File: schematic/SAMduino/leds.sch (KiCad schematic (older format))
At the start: 32 parts, among them J10 Conn_02x11_Odd_Even, J11 Conn_02x09_Odd_Even, J12 Conn_02x09_Odd_Even, J13 Conn_01x02, J14 Conn_02x02_Odd_Even, J15 Conn_02x03_Odd_Even, J16 Conn_01x02, J17 Conn_02x03_Odd_Even, J18 Conn_02x02_Odd_Even, J19 Conn_02x03_Odd_Even, J20 Conn_01x08, J7 Conn_01x02, J8 Conn_01x02, J9 Conn_02x07_Odd_Even, SW1 SW_MEC_5E, SW2 SW_MEC_5E, SW3 MCLR, SW4 ERASE

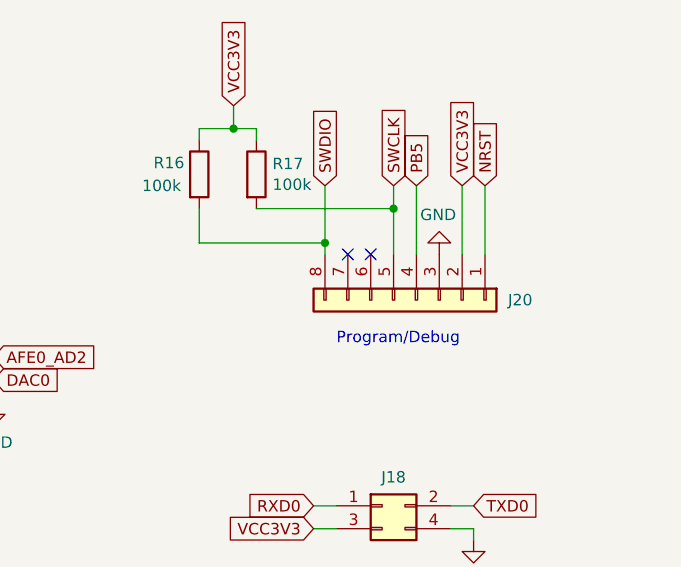
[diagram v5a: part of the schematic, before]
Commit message: Swapped program header to match PicKit4
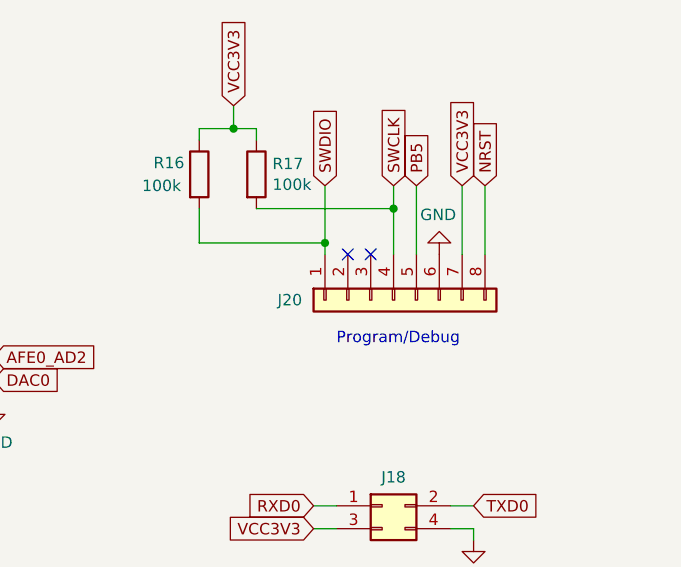
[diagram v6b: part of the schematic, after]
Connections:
- net GND: now also J20.6 (Pin_6); no longer J20.3 (Pin_3)
- net NRST: now also J20.8 (Pin_8); no longer J20.1 (Pin_1)
- net PB5: now also J20.5 (Pin_5); no longer J20.4 (Pin_4)
- net SWCLK: now also J20.4 (Pin_4); no longer J20.5 (Pin_5)
- net SWDIO: now also J20.1 (Pin_1); no longer J20.8 (Pin_8)
- net VCC3V3: now also J20.7 (Pin_7); no longer J20.2 (Pin_2)
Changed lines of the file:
@@
 L Connector_Generic:Conn_01x08 J20
 U 1 1 6166979A
-P 9350 3750
-F 0 "J20" V 9350 4150 50  0000 L CNN
-F 1 "Conn_01x08" H 9430 3651 50  0001 L CNN
-F 2 "Connector_PinHeader_2.54mm:PinHeader_1x08_P2.54mm_Horizontal" H 9350 3750 50  0001 C CNN
-F 3 "~" H 9350 3750 50  0001 C CNN
-	1    9350 3750
-	0    1    1    0
+P 9250 3750
+F 0 "J20" V 9250 4150 50  0000 L CNN
+F 1 "Conn_01x08" H 9330 3651 50  0001 L CNN
+F 2 "Connector_PinHeader_2.54mm:PinHeader_1x08_P2.54mm_Horizontal" H 9250 3750 50  0001 C CNN
+F 3 "~" H 9250 3750 50  0001 C CNN
+	1    9250 3750
+	0    -1   1    0
 $EndComp
 Text Notes 9000 3950 0    50   ~ 0

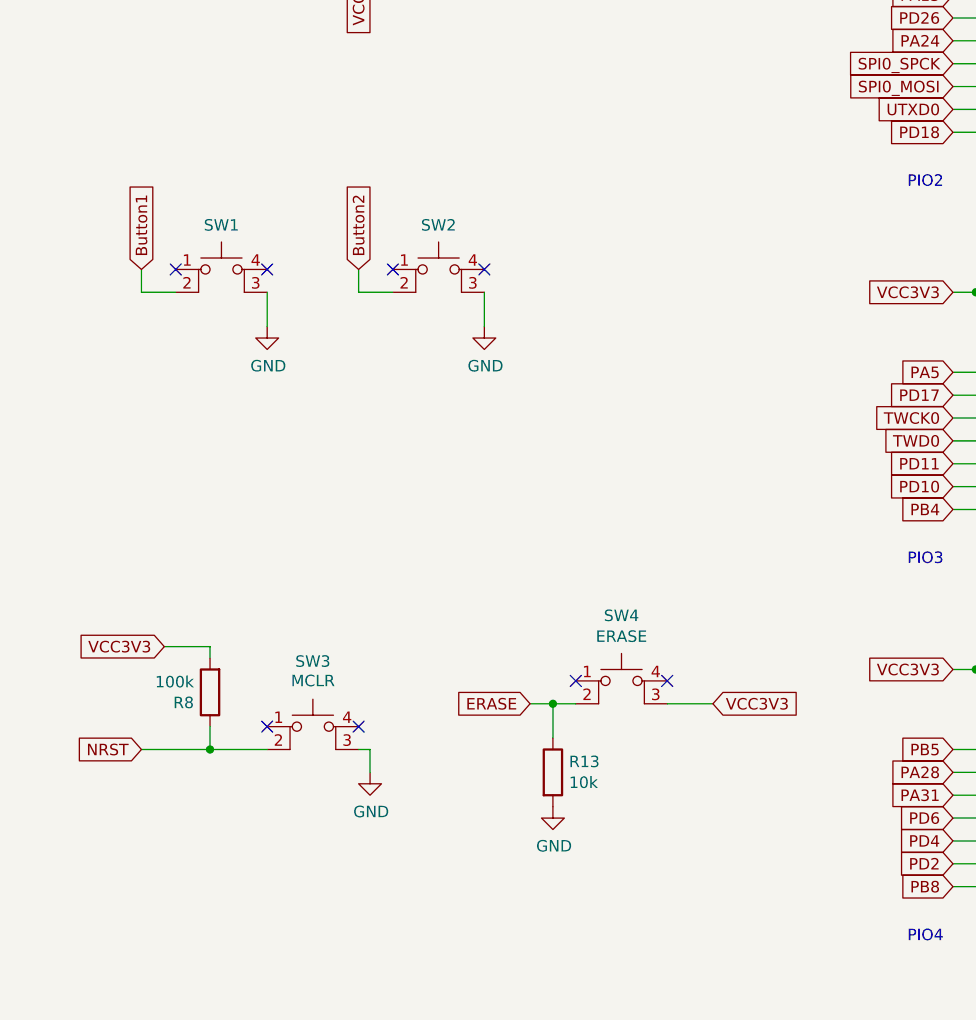
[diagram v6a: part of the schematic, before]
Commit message: Full PCB layout
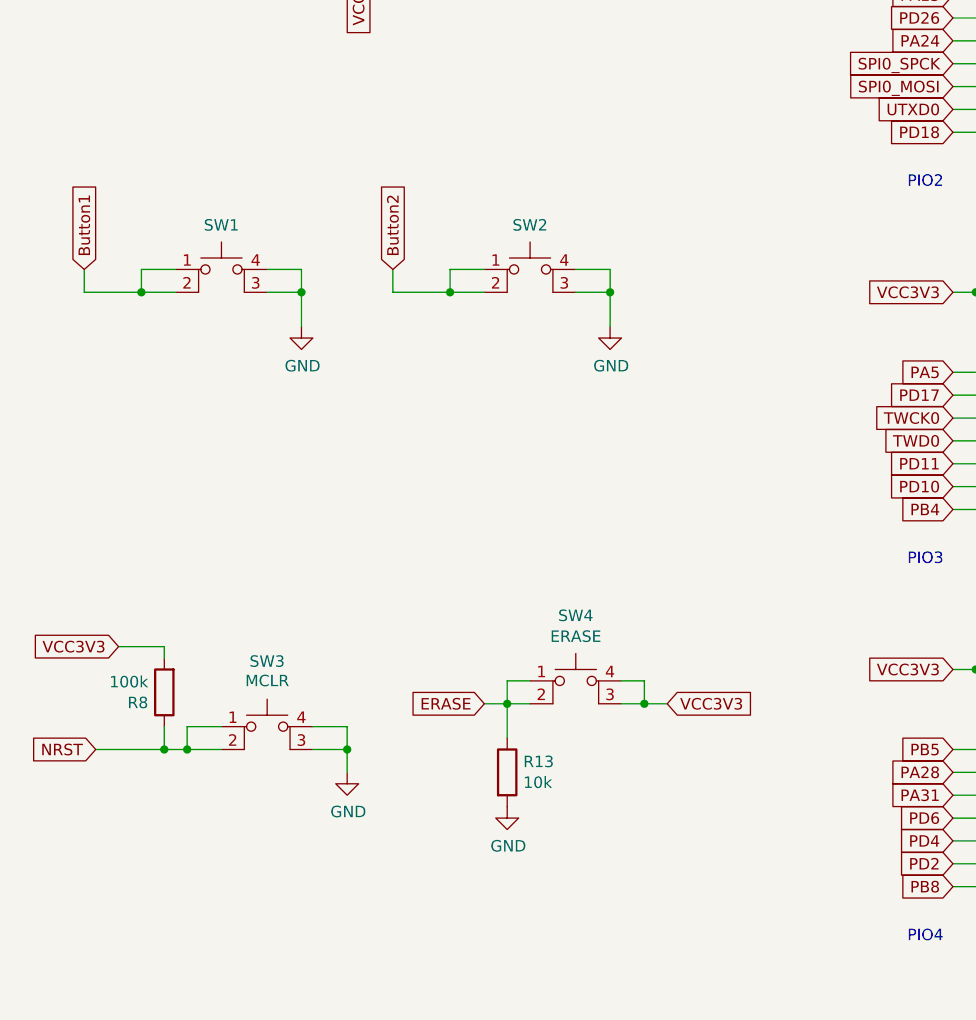
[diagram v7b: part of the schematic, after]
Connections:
- net Button1: now also SW1.1
- net Button2: now also SW2.1
- net ERASE: now also SW4.1
- net GND: now also SW1.4 (A), SW2.4 (A), SW3.4 (A)
- net NRST: now also SW3.1
- net VCC3V3: now also SW4.4 (A)
- no-connect marks 10 -> 2
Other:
- moved on the sheet: R13, R8, SW2, SW3, SW4
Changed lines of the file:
@@
 L Device:R R8
 U 1 1 61656110
-P 1450 5800
-F 0 "R8" H 1520 5846 50  0000 L CNN
-F 1 "100k" H 1520 5755 50  0000 L CNN
-F 2 "Resistor_SMD:R_0603_1608Metric" V 1380 5800 50  0001 C CNN
-F 3 "~" H 1450 5800 50  0001 C CNN
-	1    1450 5800
+P 1250 5800
+F 0 "R8" H 1320 5846 50  0000 L CNN
+F 1 "100k" H 1320 5755 50  0000 L CNN
+F 2 "Resistor_SMD:R_0603_1608Metric" V 1180 5800 50  0001 C CNN
+F 3 "~" H 1250 5800 50  0001 C CNN
+	1    1250 5800
 	-1   0    0    1
 $EndComp
@@
 L Device:R R13
 U 1 1 616567F6
-P 2950 6150
-F 0 "R13" H 3020 6196 50  0000 L CNN
-F 1 "10k" H 3020 6105 50  0000 L CNN
-F 2 "Resistor_SMD:R_0603_1608Metric" V 2880 6150 50  0001 C CNN
-F 3 "~" H 2950 6150 50  0001 C CNN
-	1    2950 6150
+P 2750 6150
+F 0 "R13" H 2820 6196 50  0000 L CNN
+F 1 "10k" H 2820 6105 50  0000 L CNN
+F 2 "Resistor_SMD:R_0603_1608Metric" V 2680 6150 50  0001 C CNN
+F 3 "~" H 2750 6150 50  0001 C CNN
+	1    2750 6150
 	1    0    0    -1
 $EndComp
@@
 	2650 1250 2650 1050
 $Comp
-L power:GND #PWR041
-U 1 1 61639104
-P 2650 4200
-F 0 "#PWR041" H 2650 3950 50  0001 C CNN
-F 1 "GND" H 2655 4027 50  0000 C CNN
-F 2 "" H 2650 4200 50  0001 C CNN
-F 3 "" H 2650 4200 50  0001 C CNN
-	1    2650 4200
-	1    0    0    -1
-$EndComp
-Wire Wire Line
-	2650 4050 2650 4200
-$Comp
 L power:GND #PWR039
 U 1 1 61639BC6
-P 1700 4200
-F 0 "#PWR039" H 1700 3950 50  0001 C CNN
-F 1 "GND" H 1705 4027 50  0000 C CNN
-F 2 "" H 1700 4200 50  0001 C CNN
-F 3 "" H 1700 4200 50  0001 C CNN
-	1    1700 4200
-	1    0    0    -1
-$EndComp
-Wire Wire Line
-	1700 4050 1700 4200
-Text GLabel 1150 3950 1    50   Input ~ 0
+P 1850 4200
+F 0 "#PWR039" H 1850 3950 50  0001 C CNN
+F 1 "GND" H 1855 4027 50  0000 C CNN
+F 2 "" H 1850 4200 50  0001 C CNN
+F 3 "" H 1850 4200 50  0001 C CNN
+	1    1850 4200
+	1    0    0    -1
+$EndComp
+Wire Wire Line
+	1850 4050 1850 4200
+Text GLabel 900  3950 1    50   Input ~ 0
 Button1
-Text GLabel 2100 3950 1    50   Input ~ 0
+Text GLabel 2250 3950 1    50   Input ~ 0
 Button2
 $Comp
 L power:GND #PWR040
 U 1 1 6163E102
-P 2150 6150
-F 0 "#PWR040" H 2150 5900 50  0001 C CNN
-F 1 "GND" H 2155 5977 50  0000 C CNN
-F 2 "" H 2150 6150 50  0001 C CNN
-F 3 "" H 2150 6150 50  0001 C CNN
-	1    2150 6150
-	1    0    0    -1
-$EndComp
-Text GLabel 1250 5600 0    50   Input ~ 0
-VCC3V3
-Text GLabel 1150 6050 0    50   Input ~ 0
+P 2050 6150
+F 0 "#PWR040" H 2050 5900 50  0001 C CNN
+F 1 "GND" H 2055 5977 50  0000 C CNN
+F 2 "" H 2050 6150 50  0001 C CNN
+F 3 "" H 2050 6150 50  0001 C CNN
+	1    2050 6150
+	1    0    0    -1
+$EndComp
+Text GLabel 1050 5600 0    50   Input ~ 0
+VCC3V3
+Text GLabel 950  6050 0    50   Input ~ 0
 NRST
 Wire Wire Line
-	2100 6050 2150 6050
-Wire Wire Line
-	2150 6050 2150 6150
-Wire Wire Line
-	1150 6050 1450 6050
-Wire Wire Line
-	1450 5950 1450 6050
-Wire Wire Line
-	1250 5600 1450 5600
-Wire Wire Line
-	1450 5600 1450 5650
-Text GLabel 3650 5850 2    50   Input ~ 0
-VCC3V3
-Text GLabel 2850 5850 0    50   Input ~ 0
+	950  6050 1250 6050
+Wire Wire Line
+	1250 5950 1250 6050
+Wire Wire Line
+	1050 5600 1250 5600
+Wire Wire Line
+	1250 5600 1250 5650
+Text GLabel 3450 5850 2    50   Input ~ 0
+VCC3V3
+Text GLabel 2650 5850 0    50   Input ~ 0
 ERASE
 $Comp
 L power:GND #PWR042
 U 1 1 6164499E
-P 2950 6300
-F 0 "#PWR042" H 2950 6050 50  0001 C CNN
-F 1 "GND" H 2955 6127 50  0000 C CNN
-F 2 "" H 2950 6300 50  0001 C CNN
-F 3 "" H 2950 6300 50  0001 C CNN
-	1    2950 6300
+P 2750 6300
+F 0 "#PWR042" H 2750 6050 50  0001 C CNN
+F 1 "GND" H 2755 6127 50  0000 C CNN
+F 2 "" H 2750 6300 50  0001 C CNN
+F 3 "" H 2750 6300 50  0001 C CNN
+	1    2750 6300
 	1    0    0    -1
 $EndComp
@@
 Connection ~ 8550 3000
 Wire Wire Line
-	3450 5850 3650 5850
-Wire Wire Line
-	2850 5850 2950 5850
-Wire Wire Line
-	2950 6000 2950 5850
-Connection ~ 2950 5850
-Wire Wire Line
-	2950 5850 3050 5850
+	3250 5850 3350 5850
+Wire Wire Line
+	2650 5850 2750 5850
+Wire Wire Line
+	2750 6000 2750 5850
+Connection ~ 2750 5850
+Wire Wire Line
+	2750 5850 2850 5850
 Text GLabel 6600 1750 0    50   Input ~ 0
 TWD0
@@
 L Switch:SW_MEC_5E SW4
 U 1 1 616A2681
-P 3250 5850
-F 0 "SW4" H 3250 6235 50  0000 C CNN
-F 1 "ERASE" H 3250 6144 50  0000 C CNN
-F 2 "SamacSys_Parts:PTS647SK38SMTR2LFS" H 3250 6150 50  0001 C CNN
-F 3 "http://www.apem.com/int/index.php?controller=attachment&id_attachment=1371" H 3250 6150 50  0001 C CNN
-	1    3250 5850
-	1    0    0    -1
-$EndComp
-$Comp
-L Switch:SW_MEC_5E SW3
-U 1 1 616B6278
-P 1900 6050
-F 0 "SW3" H 1900 6435 50  0000 C CNN
-F 1 "MCLR" H 1900 6350 50  0000 C CNN
-F 2 "SamacSys_Parts:PTS647SK38SMTR2LFS" H 1900 6350 50  0001 C CNN
-F 3 "http://www.apem.com/int/index.php?controller=attachment&id_attachment=1371" H 1900 6350 50  0001 C CNN
-	1    1900 6050
+P 3050 5850
+F 0 "SW4" H 3050 6235 50  0000 C CNN
+F 1 "ERASE" H 3050 6144 50  0000 C CNN
+F 2 "SamacSys_Parts:PTS647SK38SMTR2LFS" H 3050 6150 50  0001 C CNN
+F 3 "http://www.apem.com/int/index.php?controller=attachment&id_attachment=1371" H 3050 6150 50  0001 C CNN
+	1    3050 5850
 	1    0    0    -1
 $EndComp
@@
 L Switch:SW_MEC_5E SW2
 U 1 1 616C4A6F
-P 2450 4050
-F 0 "SW2" H 2450 4343 50  0000 C CNN
-F 1 "SW_MEC_5E" H 2450 4344 50  0001 C CNN
-F 2 "SamacSys_Parts:FSM16JH" H 2450 4350 50  0001 C CNN
-F 3 "http://www.apem.com/int/index.php?controller=attachment&id_attachment=1371" H 2450 4350 50  0001 C CNN
-	1    2450 4050
-	1    0    0    -1
-$EndComp
-Wire Wire Line
-	1300 4050 1150 4050
-Wire Wire Line
-	1150 4050 1150 3950
-Wire Wire Line
-	2250 4050 2100 4050
-Wire Wire Line
-	2100 4050 2100 3950
-NoConn ~ 1700 5950
-NoConn ~ 2100 5950
-NoConn ~ 3050 5750
-NoConn ~ 3450 5750
-NoConn ~ 1700 3950
-NoConn ~ 1300 3950
-NoConn ~ 2250 3950
-NoConn ~ 2650 3950
-Connection ~ 1450 6050
-Wire Wire Line
-	1450 6050 1700 6050
+P 2850 4050
+F 0 "SW2" H 2850 4343 50  0000 C CNN
+F 1 "SW_MEC_5E" H 2850 4344 50  0001 C CNN
+F 2 "SamacSys_Parts:FSM16JH" H 2850 4350 50  0001 C CNN
+F 3 "http://www.apem.com/int/index.php?controller=attachment&id_attachment=1371" H 2850 4350 50  0001 C CNN
+	1    2850 4050
+	1    0    0    -1
+$EndComp
+Connection ~ 1250 6050
+Wire Wire Line
+	1250 6050 1350 6050
+$Comp
+L Switch:SW_MEC_5E SW3
+U 1 1 616B6278
+P 1700 6050
+F 0 "SW3" H 1700 6435 50  0000 C CNN
+F 1 "MCLR" H 1700 6350 50  0000 C CNN
+F 2 "SamacSys_Parts:PTS647SK38SMTR2LFS" H 1700 6350 50  0001 C CNN
+F 3 "http://www.apem.com/int/index.php?controller=attachment&id_attachment=1371" H 1700 6350 50  0001 C CNN
+	1    1700 6050
+	1    0    0    -1
+$EndComp
+Wire Wire Line
+	2050 6050 2050 6150
+Wire Wire Line
+	1900 6050 2050 6050
+Wire Wire Line
+	1900 5950 2050 5950
+Wire Wire Line
+	2050 5950 2050 6050
+Connection ~ 2050 6050
+Wire Wire Line
+	1500 5950 1350 5950
+Wire Wire Line
+	1350 5950 1350 6050
+Connection ~ 1350 6050
+Wire Wire Line
+	1350 6050 1500 6050
+Wire Wire Line
+	2850 5750 2750 5750
+Wire Wire Line
+	2750 5750 2750 5850
+Wire Wire Line
+	3250 5750 3350 5750
+Wire Wire Line
+	3350 5750 3350 5850
+Connection ~ 3350 5850
+Wire Wire Line
+	3350 5850 3450 5850
+Wire Wire Line
+	900  4050 900  3950
+Wire Wire Line
+	900  4050 1150 4050
+Wire Wire Line
+	1300 3950 1150 3950
+Wire Wire Line
+	1150 3950 1150 4050
+Connection ~ 1150 4050
+Wire Wire Line
+	1150 4050 1300 4050
+Wire Wire Line
+	1700 4050 1850 4050
+Wire Wire Line
+	1700 3950 1850 3950
+Wire Wire Line
+	1850 3950 1850 4050
+Connection ~ 1850 4050
+Wire Wire Line
+	2650 4050 2500 4050
+Wire Wire Line
+	2250 4050 2250 3950
+Wire Wire Line
+	2650 3950 2500 3950
+Wire Wire Line
+	2500 3950 2500 4050
+Connection ~ 2500 4050
+Wire Wire Line
+	2500 4050 2250 4050
+$Comp
+L power:GND #PWR041
+U 1 1 61639104
+P 3200 4200
+F 0 "#PWR041" H 3200 3950 50  0001 C CNN
+F 1 "GND" H 3205 4027 50  0000 C CNN
+F 2 "" H 3200 4200 50  0001 C CNN
+F 3 "" H 3200 4200 50  0001 C CNN
+	1    3200 4200
+	1    0    0    -1
+$EndComp
+Wire Wire Line
+	3050 4050 3200 4050
+Wire Wire Line
+	3200 4050 3200 4200
+Wire Wire Line
+	3050 3950 3200 3950
+Wire Wire Line
+	3200 3950 3200 4050
+Connection ~ 3200 4050
 $EndSCHEMATC
